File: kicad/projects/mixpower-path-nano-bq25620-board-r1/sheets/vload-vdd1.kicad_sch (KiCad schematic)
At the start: 13 parts, among them Q8 SIA931DJ, Q9 Si1026X

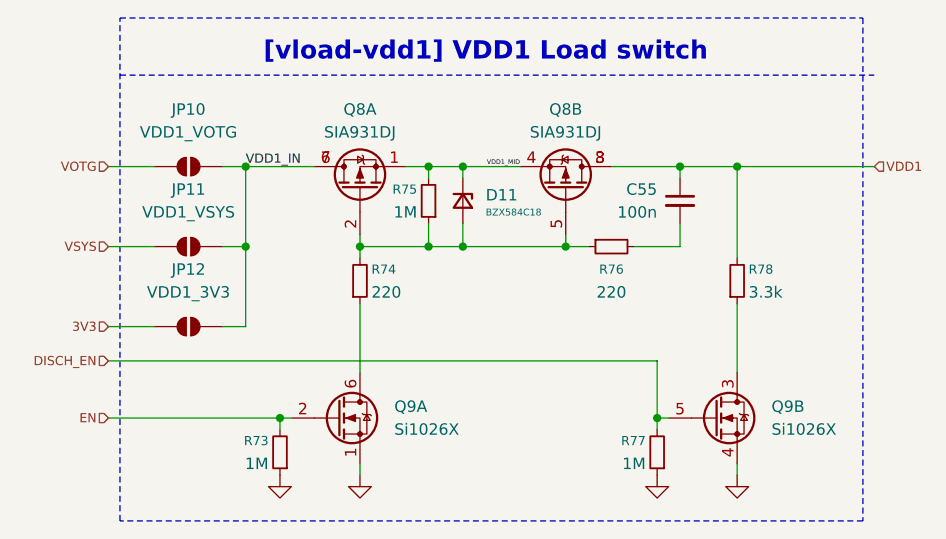
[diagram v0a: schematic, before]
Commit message: feat: rework schematics and add proper calculations
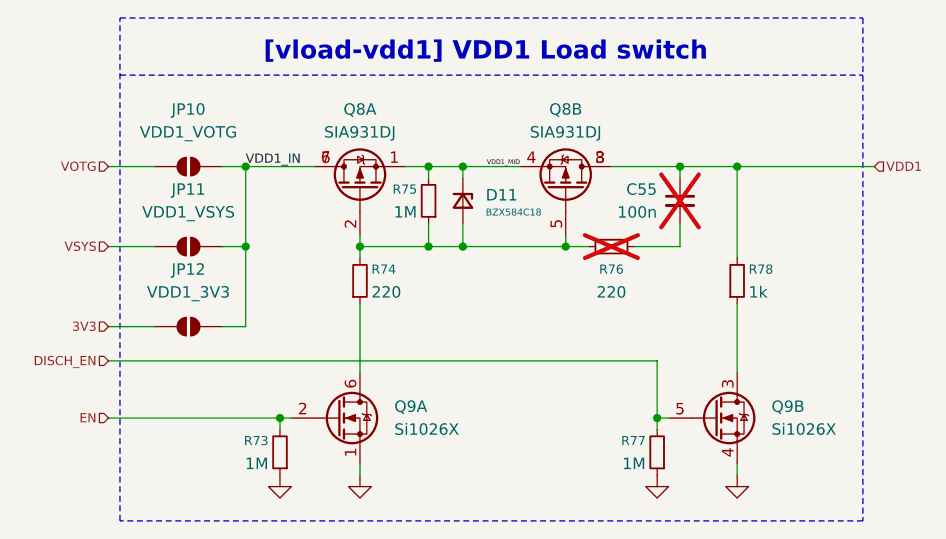
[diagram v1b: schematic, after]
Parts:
- C55, R76: now not fitted
- R74: footprint Resistor_SMD:R_0402_1005Metric -> Resistor_SMD:R_0805_2012Metric
- R78: value 3.3k -> 1k; footprint Resistor_SMD:R_1206_3216Metric -> Resistor_SMD:R_1210_3225Metric
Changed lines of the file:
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@@
 	(polyline
 		(pts
-			(xy 92.71 64.77) (xy 176.53 64.77)
+			(xy 92.71 64.77) (xy 175.26 64.77)
 		)
 		(stroke
@@
 			)
 		)
-		(property "Value" "3.3k"
+		(property "Value" "1k"
 			(at 162.56 88.8999 0)
 			(show_name no)
@@
 			)
 		)
-		(property "Footprint" "Resistor_SMD:R_1206_3216Metric"
+		(property "Footprint" "Resistor_SMD:R_1210_3225Metric"
 			(at 161.29 87.63 0)
 			(hide yes)
@@
 		)
 		(instances
-			(project "mixpower-path-mini-bq25620-board-r1"
+			(project "mixpower-path-nano-bq25620-board-r1"
 				(path "/2e43857b-9bf9-460c-948c-ec2cf8a8d6b4/58d5e6bb-811f-45d3-aa67-b144100f4607"
 					(reference "R78")
@@
 		(on_board yes)
 		(in_pos_files yes)
-		(dnp no)
+		(dnp yes)
 		(property "Reference" "C55"
 			(at 152.4 77.4762 0)
@@
 		)
 		(instances
-			(project "mixpower-path-mini-bq25620-board-r1"
+			(project "mixpower-path-nano-bq25620-board-r1"
 				(path "/2e43857b-9bf9-460c-948c-ec2cf8a8d6b4/58d5e6bb-811f-45d3-aa67-b144100f4607"
 					(reference "C55")
@@
 		)
 		(instances
-			(project "mixpower-path-mini-bq25620-board-r1"
+			(project "mixpower-path-nano-bq25620-board-r1"
 				(path "/2e43857b-9bf9-460c-948c-ec2cf8a8d6b4/58d5e6bb-811f-45d3-aa67-b144100f4607"
 					(reference "#PWR095")
@@
 		)
 		(instances
-			(project "mixpower-path-mini-bq25620-board-r1"
+			(project "mixpower-path-nano-bq25620-board-r1"
 				(path "/2e43857b-9bf9-460c-948c-ec2cf8a8d6b4/58d5e6bb-811f-45d3-aa67-b144100f4607"
 					(reference "Q8")
@@
 		)
 		(instances
-			(project "mixpower-path-mini-bq25620-board-r1"
+			(project "mixpower-path-nano-bq25620-board-r1"
 				(path "/2e43857b-9bf9-460c-948c-ec2cf8a8d6b4/58d5e6bb-811f-45d3-aa67-b144100f4607"
 					(reference "R73")
@@
 		)
 		(instances
-			(project "mixpower-path-mini-bq25620-board-r1"
+			(project "mixpower-path-nano-bq25620-board-r1"
 				(path "/2e43857b-9bf9-460c-948c-ec2cf8a8d6b4/58d5e6bb-811f-45d3-aa67-b144100f4607"
 					(reference "#PWR093")
@@
 		(on_board yes)
 		(in_pos_files yes)
-		(dnp no)
+		(dnp yes)
 		(fields_autoplaced yes)
 		(property "Reference" "R76"
@@
 		)
 		(instances
-			(project "mixpower-path-mini-bq25620-board-r1"
+			(project "mixpower-path-nano-bq25620-board-r1"
 				(path "/2e43857b-9bf9-460c-948c-ec2cf8a8d6b4/58d5e6bb-811f-45d3-aa67-b144100f4607"
 					(reference "R76")
@@
 		)
 		(instances
-			(project "mixpower-path-mini-bq25620-board-r1"
+			(project "mixpower-path-nano-bq25620-board-r1"
 				(path "/2e43857b-9bf9-460c-948c-ec2cf8a8d6b4/58d5e6bb-811f-45d3-aa67-b144100f4607"
 					(reference "R77")
@@
 		)
 		(instances
-			(project "mixpower-path-mini-bq25620-board-r1"
+			(project "mixpower-path-nano-bq25620-board-r1"
 				(path "/2e43857b-9bf9-460c-948c-ec2cf8a8d6b4/58d5e6bb-811f-45d3-aa67-b144100f4607"
 					(reference "JP12")
@@
 		)
 		(instances
-			(project "mixpower-path-mini-bq25620-board-r1"
+			(project "mixpower-path-nano-bq25620-board-r1"
 				(path "/2e43857b-9bf9-460c-948c-ec2cf8a8d6b4/58d5e6bb-811f-45d3-aa67-b144100f4607"
 					(reference "#PWR096")
@@
 		)
 		(instances
-			(project "mixpower-path-mini-bq25620-board-r1"
+			(project "mixpower-path-nano-bq25620-board-r1"
 				(path "/2e43857b-9bf9-460c-948c-ec2cf8a8d6b4/58d5e6bb-811f-45d3-aa67-b144100f4607"
 					(reference "R75")
@@
 		)
 		(instances
-			(project "mixpower-path-mini-bq25620-board-r1"
+			(project "mixpower-path-nano-bq25620-board-r1"
 				(path "/2e43857b-9bf9-460c-948c-ec2cf8a8d6b4/58d5e6bb-811f-45d3-aa67-b144100f4607"
 					(reference "JP11")
@@
 			)
 		)
-		(property "Footprint" "Resistor_SMD:R_0402_1005Metric"
+		(property "Footprint" "Resistor_SMD:R_0805_2012Metric"
 			(at 119.38 87.63 0)
 			(hide yes)
@@
 		)
 		(instances
-			(project "mixpower-path-mini-bq25620-board-r1"
+			(project "mixpower-path-nano-bq25620-board-r1"
 				(path "/2e43857b-9bf9-460c-948c-ec2cf8a8d6b4/58d5e6bb-811f-45d3-aa67-b144100f4607"
 					(reference "R74")
@@
 		)
 		(instances
-			(project "mixpower-path-mini-bq25620-board-r1"
+			(project "mixpower-path-nano-bq25620-board-r1"
 				(path "/2e43857b-9bf9-460c-948c-ec2cf8a8d6b4/58d5e6bb-811f-45d3-aa67-b144100f4607"
 					(reference "Q9")
@@
 		)
 		(instances
-			(project "mixpower-path-mini-bq25620-board-r1"
+			(project "mixpower-path-nano-bq25620-board-r1"
 				(path "/2e43857b-9bf9-460c-948c-ec2cf8a8d6b4/58d5e6bb-811f-45d3-aa67-b144100f4607"
 					(reference "D11")
@@
 		)
 		(instances
-			(project "mixpower-path-mini-bq25620-board-r1"
+			(project "mixpower-path-nano-bq25620-board-r1"
 				(path "/2e43857b-9bf9-460c-948c-ec2cf8a8d6b4/58d5e6bb-811f-45d3-aa67-b144100f4607"
 					(reference "Q8")
@@
 		)
 		(instances
-			(project "mixpower-path-mini-bq25620-board-r1"
+			(project "mixpower-path-nano-bq25620-board-r1"
 				(path "/2e43857b-9bf9-460c-948c-ec2cf8a8d6b4/58d5e6bb-811f-45d3-aa67-b144100f4607"
 					(reference "JP10")
@@
 		)
 		(instances
-			(project "mixpower-path-mini-bq25620-board-r1"
+			(project "mixpower-path-nano-bq25620-board-r1"
 				(path "/2e43857b-9bf9-460c-948c-ec2cf8a8d6b4/58d5e6bb-811f-45d3-aa67-b144100f4607"
 					(reference "Q9")
@@
 		)
 		(instances
-			(project "mixpower-path-mini-bq25620-board-r1"
+			(project "mixpower-path-nano-bq25620-board-r1"
 				(path "/2e43857b-9bf9-460c-948c-ec2cf8a8d6b4/58d5e6bb-811f-45d3-aa67-b144100f4607"
 					(reference "#PWR094")
